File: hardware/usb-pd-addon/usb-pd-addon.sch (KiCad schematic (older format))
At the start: 61 parts, among them J1 Conn_02x10_Odd_Even, J10 Conn_01x03_Male, J11 Conn_01x03_Male, J12 Conn_01x03_Male, J2 Conn_02x10_Odd_Even, J3 USB_TYPE_C, J4 USB_TYPE_C, J5 Conn_01x03_Male, J6 TPAS, J7 TPBS, J8 Conn_02x03_Odd_Even, U1 FUSB302B, U2 AP2171W, U3 SN74AVC1T45DBVR, U4 SN74AVC1T45DBVR, U5 SN74AVC1T45DBVR, U6 SN74AVC1T45DBVR, U7 AP2127K-ADJ

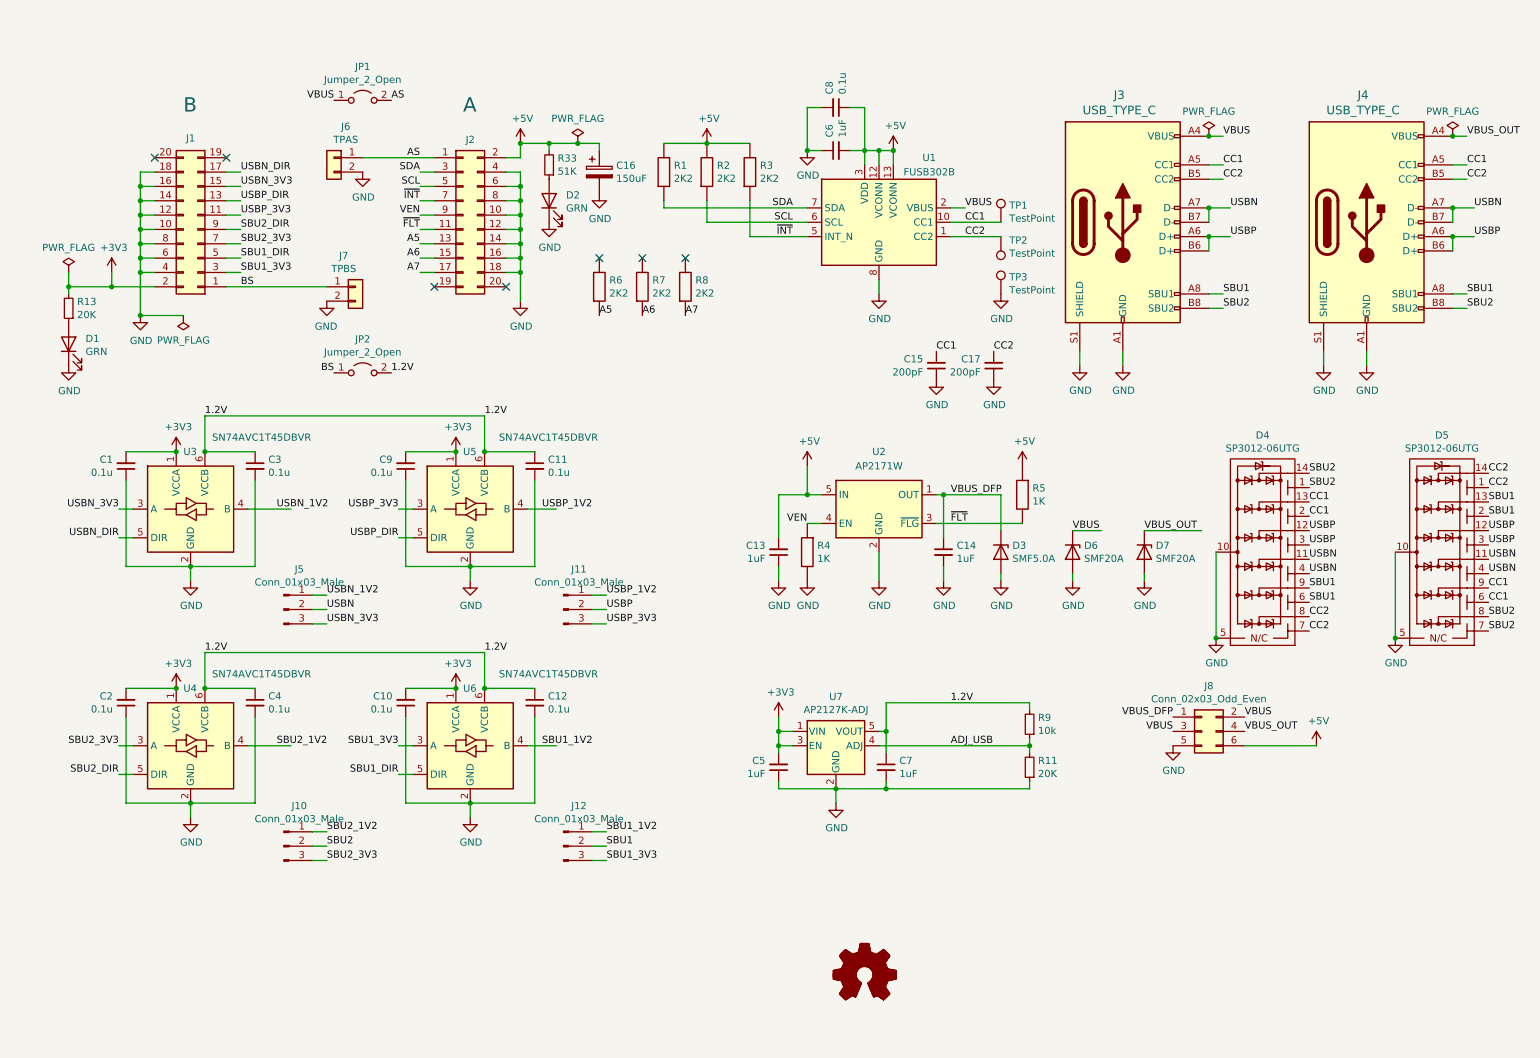
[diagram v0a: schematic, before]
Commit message: v0.7a: analog switches instead of jumpers
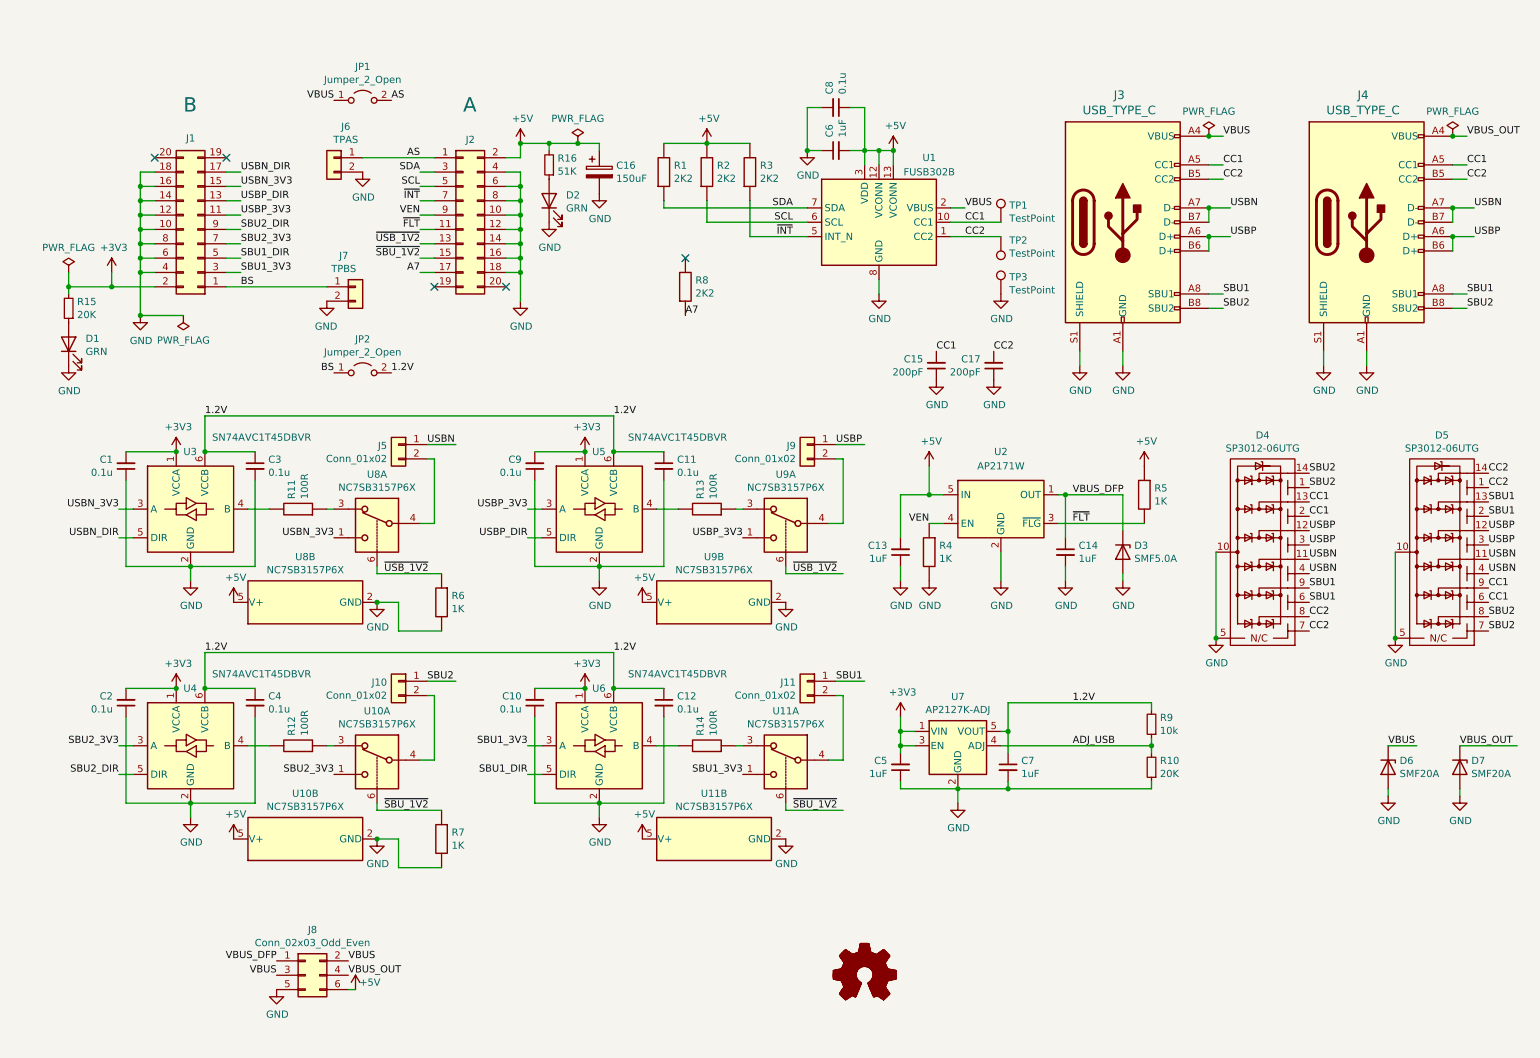
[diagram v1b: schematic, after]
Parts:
- removed J10, J11, J12, J5: Conn_01x03_Male, Connector_PinHeader_2.54mm:PinHeader_1x03_P2.54mm_Vertical, symbol Connector:Conn_01x03_Male
- added J10, J11, J5, J9: Conn_01x02, Connector_PinHeader_2.54mm:PinHeader_1x02_P2.54mm_Vertical, symbol Connector_Generic:Conn_01x02
- added R11, R12, R13, R14: 100R, pkl_dipol:R_0603, symbol pkl_device:pkl_R
- added U10, U11, U8, U9: NC7SB3157P6X, Package_TO_SOT_SMD:SOT-363_SC-70-6, symbol Analog_Switch:NC7SB3157P6X
- R6, R7: value 2K2 -> 1K; LCSC C4190 -> C21190
- renumbered R11 to R10, R13 to R15, R33 to R16
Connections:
- net labels added: ~SBU_1V2, ~USB_1V2
- net labels removed: A5, A6, SBU1_1V2, SBU2_1V2, USBN_1V2, USBP_1V2
- wire segments 207 -> 229
- no-connect marks 7 -> 5
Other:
- moved on the sheet: C10, C11, C12, C13, C14, C5, C7, C9, D3, D6, D7, J8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

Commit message: Interim version for review
Changed level shifters to smaller footprint.
Added pull-down resistors on direction signals and analog switch selects.
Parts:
- added C18, C19, C20, C21: 0.1u, pkl_dipol:C_0603, symbol Device:C_Small
- added R17, R18, R19, R20: 100K, pkl_dipol:R_0603, symbol pkl_device:pkl_R
- R6, R7: value 1K -> 100K; LCSC C21190 -> C25803
- U3, U4, U5: value SN74AVC1T45DBVR -> SN74AVC1T45DCKR; footprint Package_TO_SOT_SMD:SOT-23-6 -> Package_TO_SOT_SMD:SOT-363_SC-70-6; symbol Logic_LevelTranslator:SN74LVC1T45DBV -> Logic_LevelTranslator:SN74LVC1T45DCK; LCSC C131978 -> C133077
- U6: footprint Package_TO_SOT_SMD:SOT-23-6 -> Package_TO_SOT_SMD:SOT-363_SC-70-6; symbol Logic_LevelTranslator:SN74LVC1T45DBV -> Logic_LevelTranslator:SN74LVC1T45DCK; LCSC C131978 -> C133077
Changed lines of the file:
@@
 Text Label 1250 5850 2    50   ~ 0
 SBU2_DIR
-Wire Wire Line
-	1250 5850 1350 5850
 Text Label 4100 5650 2    50   ~ 0
 SBU1_3V3
@@
 SBU1_DIR
 Wire Wire Line
-	4100 5850 4200 5850
-Wire Wire Line
 	3350 2150 3450 2150
 Wire Wire Line
@@
 Text Label 4100 4200 2    50   ~ 0
 USBP_DIR
-Wire Wire Line
-	4100 4200 4200 4200
 Text Label 1250 4000 2    50   ~ 0
 USBN_3V3
@@
 	1350 4000 1250 4000
 Wire Wire Line
-	1250 4200 1350 4200
-Text Label 1250 4200 2    50   ~ 0
-USBN_DIR
-Wire Wire Line
 	6450 1500 6550 1500
 Connection ~ 6550 1500
@@
 $EndComp
 $Comp
-L Logic_LevelTranslator:SN74LVC1T45DBV U3
+L Logic_LevelTranslator:SN74LVC1T45DCK U3
 U 1 1 605FE266
 P 1750 4000
 F 0 "U3" H 1700 4400 50  0000 L CNN
-F 1 "SN74AVC1T45DBVR" H 1900 4500 50  0000 L CNN
-F 2 "Package_TO_SOT_SMD:SOT-23-6" H 1750 3200 50  0001 C CNN
+F 1 "SN74AVC1T45DCKR" H 1900 4500 50  0000 L CNN
+F 2 "Package_TO_SOT_SMD:SOT-363_SC-70-6" H 1750 3200 50  0001 C CNN
 F 3 "http://www.ti.com/lit/ds/symlink/sn74avc1t45.pdf" H 850 3350 50  0001 C CNN
-F 4 "C131978" H 1750 3100 50  0001 C CNN "LCSC"
+F 4 "C133077" H 1750 3100 50  0001 C CNN "LCSC"
 	1    1750 4000
 	1    0    0    -1
@@
 	5350 2000 6050 2000
 $Comp
-L Logic_LevelTranslator:SN74LVC1T45DBV U4
+L Logic_LevelTranslator:SN74LVC1T45DCK U4
 U 1 1 60284032
 P 1750 5650
 F 0 "U4" H 1700 6050 50  0000 L CNN
-F 1 "SN74AVC1T45DBVR" H 1900 6150 50  0000 L CNN
-F 2 "Package_TO_SOT_SMD:SOT-23-6" H 1750 4850 50  0001 C CNN
-F 3 "http://www.ti.com/lit/ds/symlink/sn74avc1t45.pdf" H 850 5000 50  0001 C CNN
-F 4 "C131978" H 1750 4750 50  0001 C CNN "LCSC"
+F 1 "SN74AVC1T45DCKR" H 1900 6150 50  0000 L CNN
+F 2 "Package_TO_SOT_SMD:SOT-363_SC-70-6" H 1750 4850 50  0001 C CNN
+F 3 "http://www.ti.com/lit/ds/symlink/sn74lvc1t45.pdf" H 850 5000 50  0001 C CNN
+F 4 "C133077" H 1750 4750 50  0001 C CNN "LCSC"
 	1    1750 5650
 	1    0    0    -1
 $EndComp
 $Comp
-L Logic_LevelTranslator:SN74LVC1T45DBV U5
+L Logic_LevelTranslator:SN74LVC1T45DCK U5
 U 1 1 60284DB1
 P 4600 4000
 F 0 "U5" H 4550 4400 50  0000 L CNN
-F 1 "SN74AVC1T45DBVR" H 4800 4500 50  0000 L CNN
-F 2 "Package_TO_SOT_SMD:SOT-23-6" H 4600 3200 50  0001 C CNN
+F 1 "SN74AVC1T45DCKR" H 4800 4500 50  0000 L CNN
+F 2 "Package_TO_SOT_SMD:SOT-363_SC-70-6" H 4600 3200 50  0001 C CNN
 F 3 "http://www.ti.com/lit/ds/symlink/sn74avc1t45.pdf" H 3700 3350 50  0001 C CNN
-F 4 "C131978" H 4600 3100 50  0001 C CNN "LCSC"
+F 4 "C133077" H 4600 3100 50  0001 C CNN "LCSC"
 	1    4600 4000
 	1    0    0    -1
 $EndComp
 $Comp
-L Logic_LevelTranslator:SN74LVC1T45DBV U6
+L Logic_LevelTranslator:SN74LVC1T45DCK U6
 U 1 1 60285CE0
 P 4600 5650
 F 0 "U6" H 4550 6050 50  0000 L CNN
 F 1 "SN74AVC1T45DBVR" H 4800 6150 50  0000 L CNN
-F 2 "Package_TO_SOT_SMD:SOT-23-6" H 4600 4850 50  0001 C CNN
-F 3 "http://www.ti.com/lit/ds/symlink/sn74avc1t45.pdf" H 3700 5000 50  0001 C CNN
-F 4 "C131978" H 4600 4750 50  0001 C CNN "LCSC"
+F 2 "Package_TO_SOT_SMD:SOT-363_SC-70-6" H 4600 4850 50  0001 C CNN
+F 3 "http://www.ti.com/lit/ds/symlink/sn74lvc1t45.pdf" H 3700 5000 50  0001 C CNN
+F 4 "C133077" H 4600 4750 50  0001 C CNN "LCSC"
 	1    4600 5650
 	1    0    0    -1
@@
 P 3500 4650
 F 0 "R6" H 3430 4604 50  0000 R CNN
-F 1 "1K" H 3430 4695 50  0000 R CNN
+F 1 "100K" H 3430 4695 50  0000 R CNN
 F 2 "pkl_dipol:R_0603" V 3430 4650 30  0001 C CNN
 F 3 "" H 3500 4650 30  0000 C CNN
-F 4 "C21190" H 3500 4650 50  0001 C CNN "LCSC"
+F 4 "C25803" H 3500 4650 50  0001 C CNN "LCSC"
 	1    3500 4650
-	-1   0    0    1
-$EndComp
-$Comp
-L pkl_device:pkl_R R7
-U 1 1 60943BE4
-P 3500 6300
-F 0 "R7" H 3430 6254 50  0000 R CNN
-F 1 "1K" H 3430 6345 50  0000 R CNN
-F 2 "pkl_dipol:R_0603" V 3430 6300 30  0001 C CNN
-F 3 "" H 3500 6300 30  0000 C CNN
-F 4 "C21190" H 3500 6300 50  0001 C CNN "LCSC"
-	1    3500 6300
 	-1   0    0    1
 $EndComp
@@
 Wire Wire Line
 	5150 5650 5000 5650
+$Comp
+L pkl_device:pkl_R R7
+U 1 1 60943BE4
+P 3500 6300
+F 0 "R7" H 3430 6254 50  0000 R CNN
+F 1 "100K" H 3430 6345 50  0000 R CNN
+F 2 "pkl_dipol:R_0603" V 3430 6300 30  0001 C CNN
+F 3 "" H 3500 6300 30  0000 C CNN
+F 4 "C25803" H 3500 6300 50  0001 C CNN "LCSC"
+	1    3500 6300
+	-1   0    0    1
+$EndComp
+$Comp
+L power:GND #PWR043
+U 1 1 603A7FF0
+P 1100 4600
+F 0 "#PWR043" H 1100 4350 50  0001 C CNN
+F 1 "GND" H 1105 4427 50  0000 C CNN
+F 2 "" H 1100 4600 50  0001 C CNN
+F 3 "" H 1100 4600 50  0001 C CNN
+	1    1100 4600
+	1    0    0    -1
+$EndComp
+$Comp
+L pkl_device:pkl_R R17
+U 1 1 603A75EE
+P 1100 4400
+F 0 "R17" H 1030 4354 50  0000 R CNN
+F 1 "100K" H 1030 4445 50  0000 R CNN
+F 2 "pkl_dipol:R_0603" V 1030 4400 30  0001 C CNN
+F 3 "" H 1100 4400 30  0000 C CNN
+F 4 "C25803" H 1100 4400 50  0001 C CNN "LCSC"
+	1    1100 4400
+	-1   0    0    1
+$EndComp
+Text Label 1250 4200 2    50   ~ 0
+USBN_DIR
+$Comp
+L power:GND #PWR044
+U 1 1 603E538D
+P 1100 6250
+F 0 "#PWR044" H 1100 6000 50  0001 C CNN
+F 1 "GND" H 1105 6077 50  0000 C CNN
+F 2 "" H 1100 6250 50  0001 C CNN
+F 3 "" H 1100 6250 50  0001 C CNN
+	1    1100 6250
+	1    0    0    -1
+$EndComp
+$Comp
+L pkl_device:pkl_R R18
+U 1 1 603E5398
+P 1100 6050
+F 0 "R18" H 1030 6004 50  0000 R CNN
+F 1 "100K" H 1030 6095 50  0000 R CNN
+F 2 "pkl_dipol:R_0603" V 1030 6050 30  0001 C CNN
+F 3 "" H 1100 6050 30  0000 C CNN
+F 4 "C25803" H 1100 6050 50  0001 C CNN "LCSC"
+	1    1100 6050
+	-1   0    0    1
+$EndComp
+$Comp
+L power:GND #PWR045
+U 1 1 603F5B02
+P 3950 4600
+F 0 "#PWR045" H 3950 4350 50  0001 C CNN
+F 1 "GND" H 3955 4427 50  0000 C CNN
+F 2 "" H 3950 4600 50  0001 C CNN
+F 3 "" H 3950 4600 50  0001 C CNN
+	1    3950 4600
+	1    0    0    -1
+$EndComp
+$Comp
+L pkl_device:pkl_R R19
+U 1 1 603F5B0D
+P 3950 4400
+F 0 "R19" H 3880 4354 50  0000 R CNN
+F 1 "100K" H 3880 4445 50  0000 R CNN
+F 2 "pkl_dipol:R_0603" V 3880 4400 30  0001 C CNN
+F 3 "" H 3950 4400 30  0000 C CNN
+F 4 "C25803" H 3950 4400 50  0001 C CNN "LCSC"
+	1    3950 4400
+	-1   0    0    1
+$EndComp
+Wire Wire Line
+	3950 4200 4200 4200
+Wire Wire Line
+	1100 4200 1350 4200
+Wire Wire Line
+	1100 5850 1350 5850
+$Comp
+L power:GND #PWR046
+U 1 1 6045EA04
+P 3950 6250
+F 0 "#PWR046" H 3950 6000 50  0001 C CNN
+F 1 "GND" H 3955 6077 50  0000 C CNN
+F 2 "" H 3950 6250 50  0001 C CNN
+F 3 "" H 3950 6250 50  0001 C CNN
+	1    3950 6250
+	1    0    0    -1
+$EndComp
+$Comp
+L pkl_device:pkl_R R20
+U 1 1 6045EA0F
+P 3950 6050
+F 0 "R20" H 3880 6004 50  0000 R CNN
+F 1 "100K" H 3880 6095 50  0000 R CNN
+F 2 "pkl_dipol:R_0603" V 3880 6050 30  0001 C CNN
+F 3 "" H 3950 6050 30  0000 C CNN
+F 4 "C25803" H 3950 6050 50  0001 C CNN "LCSC"
+	1    3950 6050
+	-1   0    0    1
+$EndComp
+Wire Wire Line
+	3950 5850 4200 5850
+$Comp
+L Device:C_Small C18
+U 1 1 6047D811
+P 2050 4750
+F 0 "C18" H 2142 4796 50  0000 L CNN
+F 1 "0.1u" H 2142 4705 50  0000 L CNN
+F 2 "pkl_dipol:C_0603" H 2050 4750 50  0001 C CNN
+F 3 "~" H 2050 4750 50  0001 C CNN
+F 4 "C14663" H 2050 4750 50  0001 C CNN "LCSC"
+	1    2050 4750
+	-1   0    0    -1
+$EndComp
+Connection ~ 2050 4650
+Connection ~ 2050 6300
+$Comp
+L Device:C_Small C21
+U 1 1 6047E71D
+P 4900 6400
+F 0 "C21" H 4992 6446 50  0000 L CNN
+F 1 "0.1u" H 4992 6355 50  0000 L CNN
+F 2 "pkl_dipol:C_0603" H 4900 6400 50  0001 C CNN
+F 3 "~" H 4900 6400 50  0001 C CNN
+F 4 "C14663" H 4900 6400 50  0001 C CNN "LCSC"
+	1    4900 6400
+	-1   0    0    -1
+$EndComp
+Connection ~ 4900 6300
+$Comp
+L Device:C_Small C20
+U 1 1 6047EC84
+P 2050 6400
+F 0 "C20" H 2142 6446 50  0000 L CNN
+F 1 "0.1u" H 2142 6355 50  0000 L CNN
+F 2 "pkl_dipol:C_0603" H 2050 6400 50  0001 C CNN
+F 3 "~" H 2050 6400 50  0001 C CNN
+F 4 "C14663" H 2050 6400 50  0001 C CNN "LCSC"
+	1    2050 6400
+	-1   0    0    -1
+$EndComp
+$Comp
+L power:GND #PWR0110
+U 1 1 6047F316
+P 2050 4850
+F 0 "#PWR0110" H 2050 4600 50  0001 C CNN
+F 1 "GND" H 2055 4677 50  0000 C CNN
+F 2 "" H 2050 4850 50  0001 C CNN
+F 3 "" H 2050 4850 50  0001 C CNN
+	1    2050 4850
+	1    0    0    -1
+$EndComp
+$Comp
+L power:GND #PWR0111
+U 1 1 6047F740
+P 2050 6500
+F 0 "#PWR0111" H 2050 6250 50  0001 C CNN
+F 1 "GND" H 2055 6327 50  0000 C CNN
+F 2 "" H 2050 6500 50  0001 C CNN
+F 3 "" H 2050 6500 50  0001 C CNN
+	1    2050 6500
+	1    0    0    -1
+$EndComp
+$Comp
+L power:GND #PWR0112
+U 1 1 6047FA6A
+P 4900 6500
+F 0 "#PWR0112" H 4900 6250 50  0001 C CNN
+F 1 "GND" H 4905 6327 50  0000 C CNN
+F 2 "" H 4900 6500 50  0001 C CNN
+F 3 "" H 4900 6500 50  0001 C CNN
+	1    4900 6500
+	1    0    0    -1
+$EndComp
+$Comp
+L power:GND #PWR0113
+U 1 1 6047FDE9
+P 4900 4850
+F 0 "#PWR0113" H 4900 4600 50  0001 C CNN
+F 1 "GND" H 4905 4677 50  0000 C CNN
+F 2 "" H 4900 4850 50  0001 C CNN
+F 3 "" H 4900 4850 50  0001 C CNN
+	1    4900 4850
+	1    0    0    -1
+$EndComp
+$Comp
+L Device:C_Small C19
+U 1 1 6047E0AE
+P 4900 4750
+F 0 "C19" H 4992 4796 50  0000 L CNN
+F 1 "0.1u" H 4992 4705 50  0000 L CNN
+F 2 "pkl_dipol:C_0603" H 4900 4750 50  0001 C CNN
+F 3 "~" H 4900 4750 50  0001 C CNN
+F 4 "C14663" H 4900 4750 50  0001 C CNN "LCSC"
+	1    4900 4750
+	-1   0    0    -1
+$EndComp
+Connection ~ 4900 4650
 $EndSCHEMATC

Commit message: v0.8a: Colocated D+/D- and SBU1/SBU2 jumpers. Moved ASA/ASB jumpers away from Glasgow headers.
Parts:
- removed J10, J5: Conn_01x02, Connector_PinHeader_2.54mm:PinHeader_1x02_P2.54mm_Vertical, symbol Connector_Generic:Conn_01x02
- J11, J9: value Conn_01x02 -> Conn_02x02; footprint Connector_PinHeader_2.54mm:PinHeader_1x02_P2.54mm_Vertical -> Connector_PinHeader_2.54mm:PinHeader_2x02_P2.54mm_Vertical; symbol Connector_Generic:Conn_01x02 -> Connector_Generic:Conn_02x02_Odd_Even
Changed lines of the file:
@@
 Title "USB-PD on Glasgow"
 Date ""
-Rev "V0.7a"
+Rev "V0.8a"
 Comp "License: CC-BY-SA 4.0"
 Comment1 "(C) 2020-2021 Piotr Esden-Tempski <piotr@esden.net>"
@@
 Wire Wire Line
 	9650 2900 9650 3000
-Text Label 3400 3550 0    50   ~ 0
+Text Label 5750 3450 2    50   ~ 0
 USBN
 Wire Wire Line
@@
 Text Label 5600 4200 2    50   ~ 0
 USBP_3V3
-Text Label 3400 5200 0    50   ~ 0
+Text Label 5750 5100 2    50   ~ 0
 SBU2
-Text Label 6250 5200 0    50   ~ 0
+Text Label 6250 5100 0    50   ~ 0
 SBU1
 Text Label 2850 7250 0    50   ~ 0
@@
 Text Label 5950 4450 0    50   ~ 0
 ~USB_1V2
-$Comp
-L Connector_Generic:Conn_01x02 J9
-U 1 1 60407FFB
-P 6050 3550
-F 0 "J9" H 6130 3542 50  0000 L CNN
-F 1 "Conn_01x02" H 6130 3451 50  0000 L CNN
-F 2 "Connector_PinHeader_2.54mm:PinHeader_1x02_P2.54mm_Vertical" H 6050 3550 50  0001 C CNN
-F 3 "~" H 6050 3550 50  0001 C CNN
-	1    6050 3550
-	-1   0    0    -1
-$EndComp
-Text Label 6250 3550 0    50   ~ 0
+Text Label 6250 3450 0    50   ~ 0
 USBP
 Wire Wire Line
-	6250 3650 6300 3650
-Wire Wire Line
-	6300 3650 6300 4100
-Wire Wire Line
-	6250 3550 6450 3550
+	6250 3550 6300 3550
 Wire Wire Line
 	5900 4400 5900 4450
@@
 ~SBU_1V2
 $Comp
-L Connector_Generic:Conn_01x02 J11
+L Connector_Generic:Conn_02x02_Odd_Even J11
 U 1 1 6057AA2A
-P 6050 5200
-F 0 "J11" H 6130 5192 50  0000 L CNN
-F 1 "Conn_01x02" H 6130 5101 50  0000 L CNN
-F 2 "Connector_PinHeader_2.54mm:PinHeader_1x02_P2.54mm_Vertical" H 6050 5200 50  0001 C CNN
-F 3 "~" H 6050 5200 50  0001 C CNN
-	1    6050 5200
+P 6050 5100
+F 0 "J11" H 6130 5092 50  0000 L CNN
+F 1 "Conn_02x02" H 6130 5001 50  0000 L CNN
+F 2 "Connector_PinHeader_2.54mm:PinHeader_2x02_P2.54mm_Vertical" H 6050 5100 50  0001 C CNN
+F 3 "~" H 6050 5100 50  0001 C CNN
+	1    6050 5100
 	-1   0    0    -1
 $EndComp
 Wire Wire Line
-	6250 5300 6300 5300
-Wire Wire Line
-	6300 5300 6300 5750
-Wire Wire Line
-	6250 5200 6450 5200
+	6250 5200 6300 5200
+Wire Wire Line
+	6250 5100 6450 5100
 Wire Wire Line
 	5900 6050 5900 6100
@@
 Text Label 3100 6100 0    50   ~ 0
 ~SBU_1V2
-$Comp
-L Connector_Generic:Conn_01x02 J10
-U 1 1 60649C48
-P 3200 5200
-F 0 "J10" H 3280 5192 50  0000 L CNN
-F 1 "Conn_01x02" H 3280 5101 50  0000 L CNN
-F 2 "Connector_PinHeader_2.54mm:PinHeader_1x02_P2.54mm_Vertical" H 3200 5200 50  0001 C CNN
-F 3 "~" H 3200 5200 50  0001 C CNN
-	1    3200 5200
-	-1   0    0    -1
-$EndComp
-Wire Wire Line
-	3400 5300 3450 5300
-Wire Wire Line
-	3450 5300 3450 5750
-Wire Wire Line
-	3400 5200 3600 5200
 Wire Wire Line
 	3050 6050 3050 6100
@@
 Text Label 3100 4450 0    50   ~ 0
 ~USB_1V2
-$Comp
-L Connector_Generic:Conn_01x02 J5
-U 1 1 606D00CE
-P 3200 3550
-F 0 "J5" H 3280 3542 50  0000 L CNN
-F 1 "Conn_01x02" H 3280 3451 50  0000 L CNN
-F 2 "Connector_PinHeader_2.54mm:PinHeader_1x02_P2.54mm_Vertical" H 3200 3550 50  0001 C CNN
-F 3 "~" H 3200 3550 50  0001 C CNN
-	1    3200 3550
-	-1   0    0    -1
-$EndComp
-Wire Wire Line
-	3400 3650 3450 3650
-Wire Wire Line
-	3450 3650 3450 4100
-Wire Wire Line
-	3400 3550 3600 3550
 Wire Wire Line
 	3050 4400 3050 4450
@@
 $EndComp
 Connection ~ 4900 4650
+Wire Wire Line
+	6300 3550 6300 4100
+Wire Wire Line
+	5750 3450 5500 3450
+$Comp
+L Connector_Generic:Conn_02x02_Odd_Even J9
+U 1 1 60407FFB
+P 6050 3450
+F 0 "J9" H 6130 3442 50  0000 L CNN
+F 1 "Conn_02x02" H 6130 3351 50  0000 L CNN
+F 2 "Connector_PinHeader_2.54mm:PinHeader_2x02_P2.54mm_Vertical" H 6050 3450 50  0001 C CNN
+F 3 "~" H 6050 3450 50  0001 C CNN
+	1    6050 3450
+	-1   0    0    -1
+$EndComp
+Wire Wire Line
+	6250 3450 6450 3450
+Wire Wire Line
+	3450 3550 5750 3550
+Wire Wire Line
+	3450 3550 3450 4100
+Wire Wire Line
+	6300 5200 6300 5750
+Wire Wire Line
+	5750 5100 5550 5100
+Wire Wire Line
+	3450 5200 5750 5200
+Wire Wire Line
+	3450 5200 3450 5750
 $EndSCHEMATC
